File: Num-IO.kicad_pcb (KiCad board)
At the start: 2 copper layers, 170.2 x 77.5 mm, 105 parts, among them J1 DB37_Female, J2 DB37_Male, J3 Conn_02x25_Odd_Even, J4 0826-1X1T-GH-F, U1 MAX14917AFM+, U10 LTC6820HMS, U11 LTC6820HMS, U12 LTC6820HMS, U2 MAX14917AFM+, U3 MAX14851AEE+, U4 MAX14917AFM+, U5 MAX31910AUI+, U6 MAX31910AUI+, U7 MAX31910AUI+, U8 MAX31910AUI+, U9 LTC6820HMS

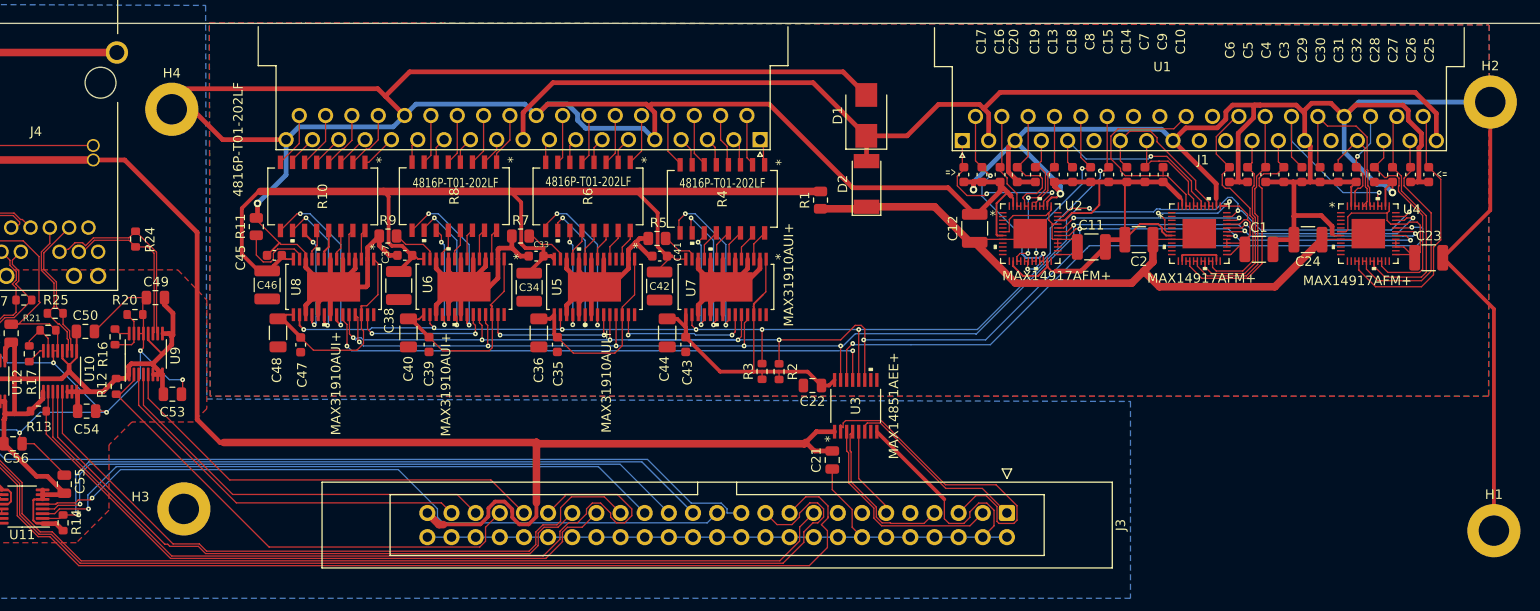
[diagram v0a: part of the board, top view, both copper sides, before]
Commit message: add missing LDO for 3.3V
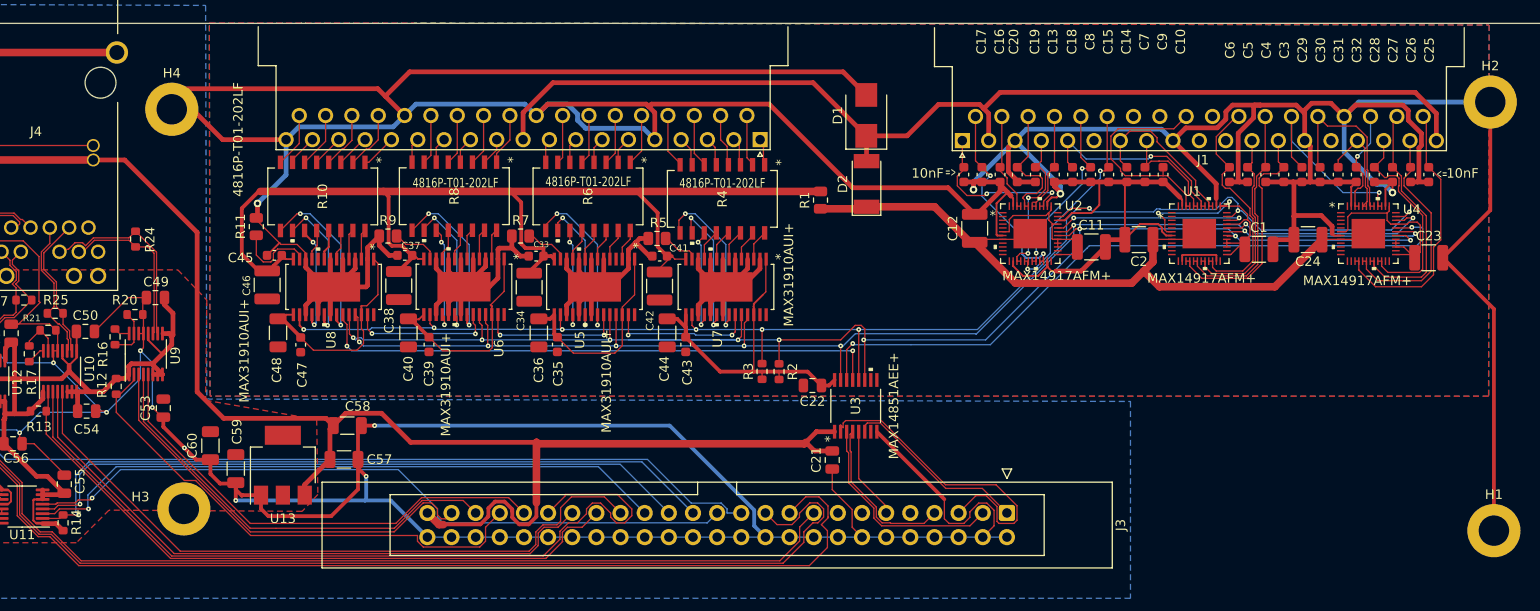
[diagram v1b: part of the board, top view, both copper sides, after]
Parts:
- added C57: 10uF, Capacitor_SMD:C_1206_3216Metric, F.Cu at (103.1, 70.1)
- added C58: 10uF, Capacitor_SMD:C_1206_3216Metric, F.Cu at (103.4, 66.5)
- added C59: 10uF, Capacitor_SMD:C_1206_3216Metric, F.Cu at (91.7, 71.1)
- added C60: 10uF, Capacitor_SMD:C_1206_3216Metric, F.Cu at (89.0, 68.7)
- added U13: AP1117-33, Package_TO_SOT_SMD:SOT-223-3_TabPin2, F.Cu at (96.6, 70.7)
- moved C53 1.75 mm to (84.1, 64.7), turned to -90 degrees
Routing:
- net GNDD: track 229.9 -> 343.2 mm, vias 7 -> 11
- net +5VD: track 139.8 -> 147.8 mm
- net /FPGA Connector/SPI4.SDO: track 40.8 -> 45.2 mm
- net /FPGA Connector/SPI4.*CS: track 47.0 -> 50.7 mm
- net /FPGA Connector/SPI4.CLK: track 42.9 -> 46.2 mm
- net +3.3V: track 107.6 -> 105.5 mm
- net /FPGA Connector/SPI4.SDI: track 52.4 -> 53.9 mm

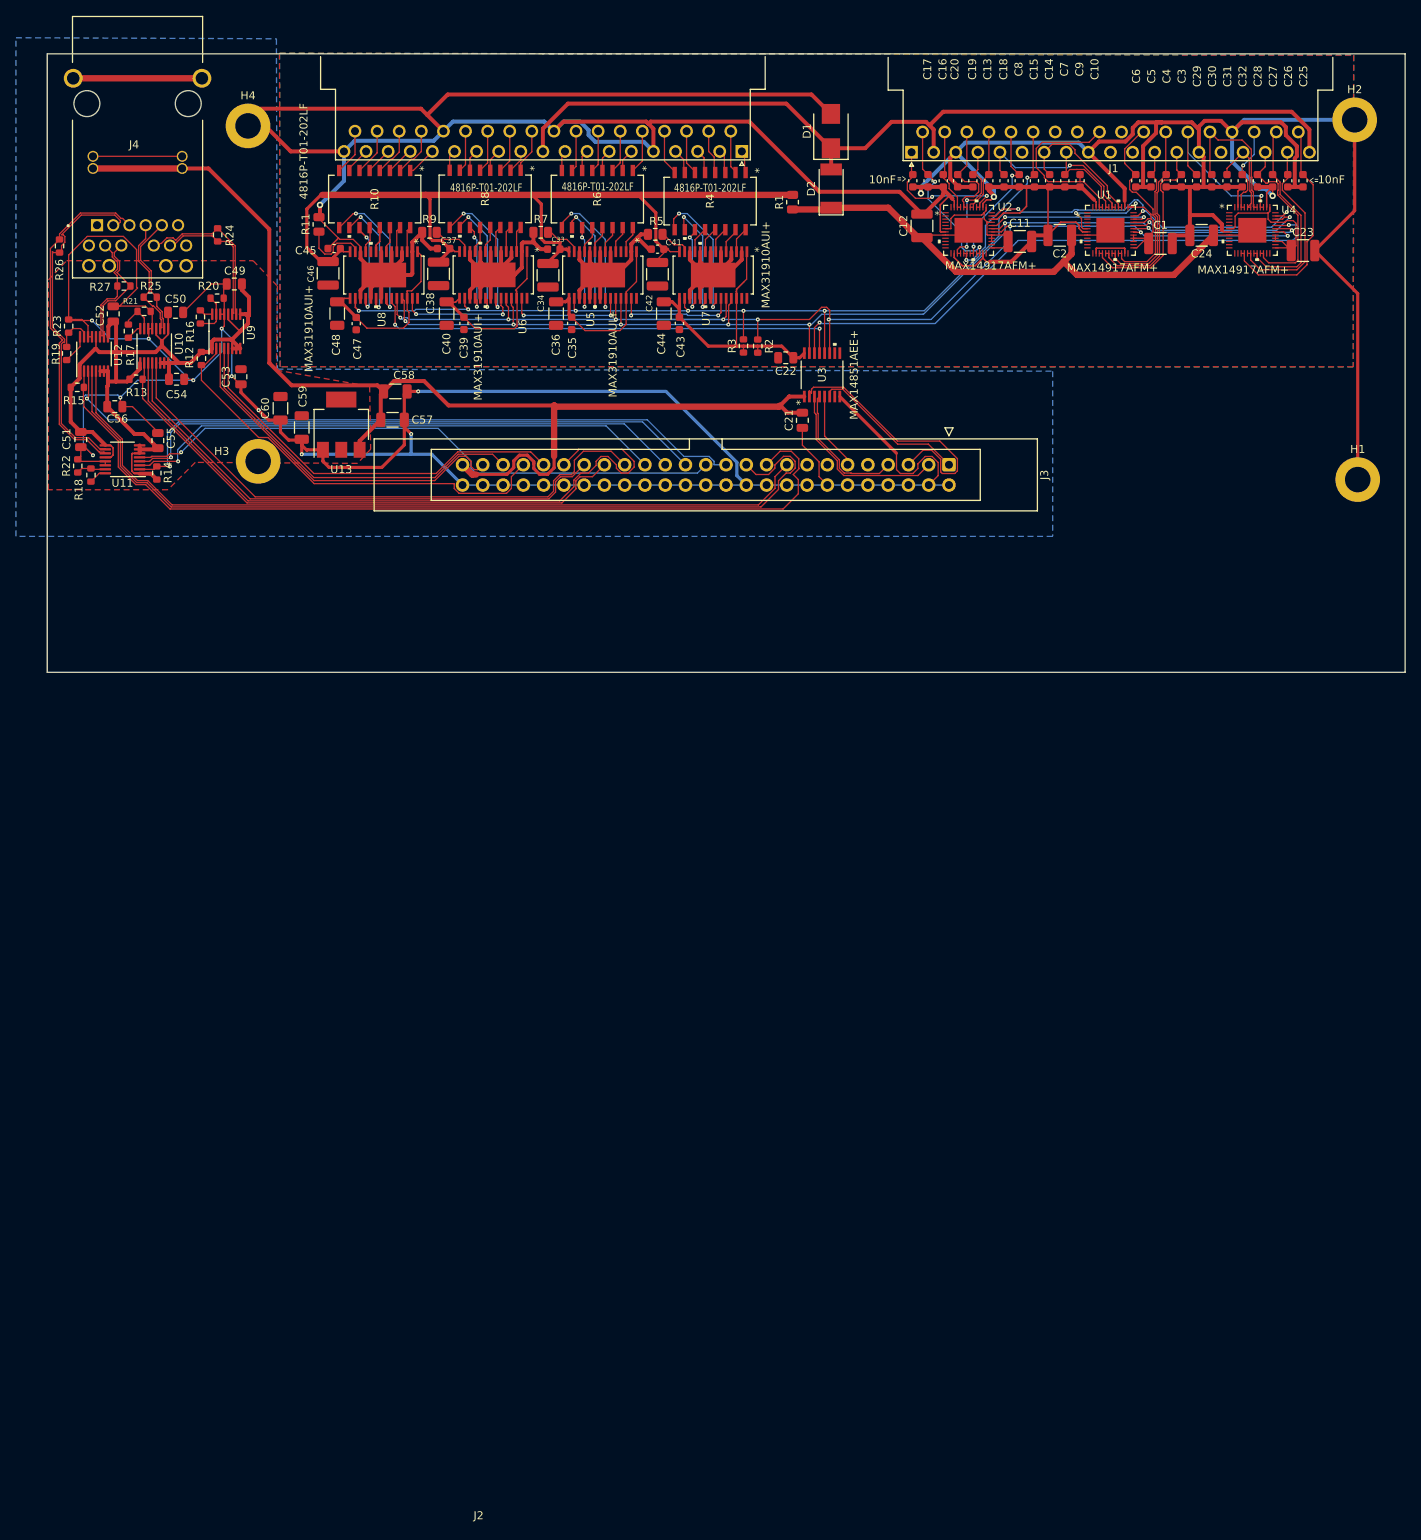
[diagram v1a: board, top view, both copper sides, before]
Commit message: fix a few warnings
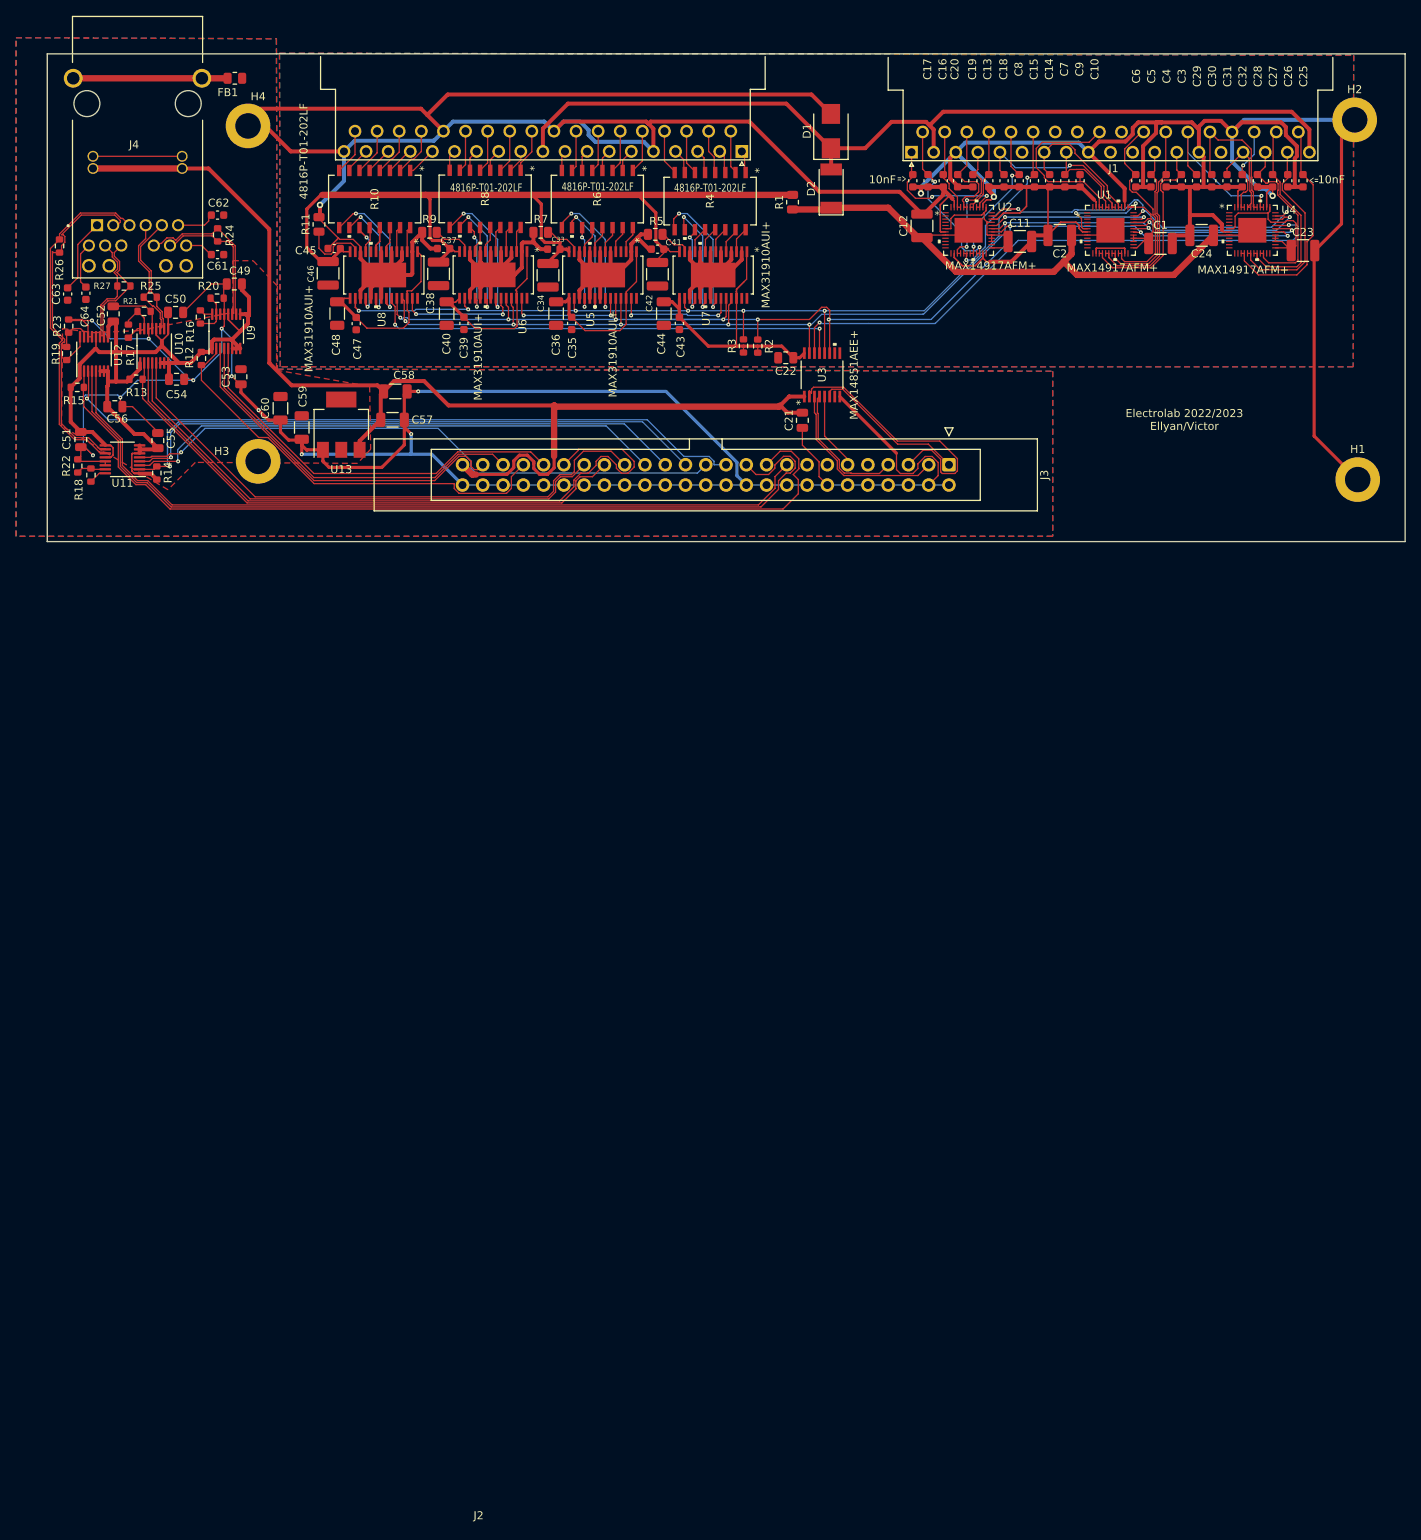
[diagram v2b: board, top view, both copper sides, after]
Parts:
- added C61: <27pF, Capacitor_SMD:C_0603_1608Metric, F.Cu at (81.1, 49.4)
- added C62: <27pF, Capacitor_SMD:C_0603_1608Metric, F.Cu at (81.1, 44.5)
- added C63: <27pF, Capacitor_SMD:C_0603_1608Metric, F.Cu at (62.4, 54.3)
- added C64: <27pF, Capacitor_SMD:C_0603_1608Metric, F.Cu at (64.6, 54.2)
- added FB1: FerriteBead, Resistor_SMD:R_0805_2012Metric, F.Cu at (83.3, 27.3)
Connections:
- net +3.3V renamed +3V3
- net Earth renamed Net-(FB1-Pad2)
- J4 pad 1: unconnected-(J4-Pad1) -> Net-(J4-Pad1)
- J4 pad 12: unconnected-(J4-Pad12) -> Net-(J4-Pad12)
- J4 pad 6: unconnected-(J4-Pad6) -> Net-(J4-Pad6)
- J4 pad 7: unconnected-(J4-Pad7) -> Net-(J4-Pad7)
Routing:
- net GNDD: track 343.2 -> 316.8 mm
- net Net-(J4-Pad1): track 0.00 -> 9.37 mm
- net Net-(J4-Pad7): track 0.00 -> 5.92 mm
- net Net-(J4-Pad6): track 0.00 -> 4.41 mm
- net Net-(J4-Pad12): track 0.00 -> 3.37 mm
- net Net-(FB1-Pad2): track 16.1 -> 19.3 mm
- added copper zone on F.Cu, net GNDD
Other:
- board size 170.2 x 77.5 mm -> 170.2 x 61.1 mm
- board text added: "Electrolab 2022/2023 Ellyan/Victor"

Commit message: fix most errors/warnings
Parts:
- added R28: 100k, Resistor_SMD:R_0603_1608Metric, F.Cu at (182.4, 44.7)
- added R29: 100k, Resistor_SMD:R_0603_1608Metric, F.Cu at (158.7, 69.7)
- added R30: 3.3k, Resistor_SMD:R_0603_1608Metric, F.Cu at (158.9, 58.8)
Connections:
- U2 pad 34: GNDPWR -> /output channel 17-24/SDO
- U3 pad 10: unconnected-(U3-Pad10) -> Net-(U3-Pad10)
- U3 pad 7: unconnected-(U3-Pad7) -> Net-(U3-Pad7)
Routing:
- net GNDPWR: track 653.7 -> 646.2 mm
- net /output channel 17-24/SDO: track 0.00 -> 3.98 mm
- net Net-(U3-Pad10): track 0.00 -> 2.28 mm
- net Net-(U3-Pad7): track 0.00 -> 2.28 mm

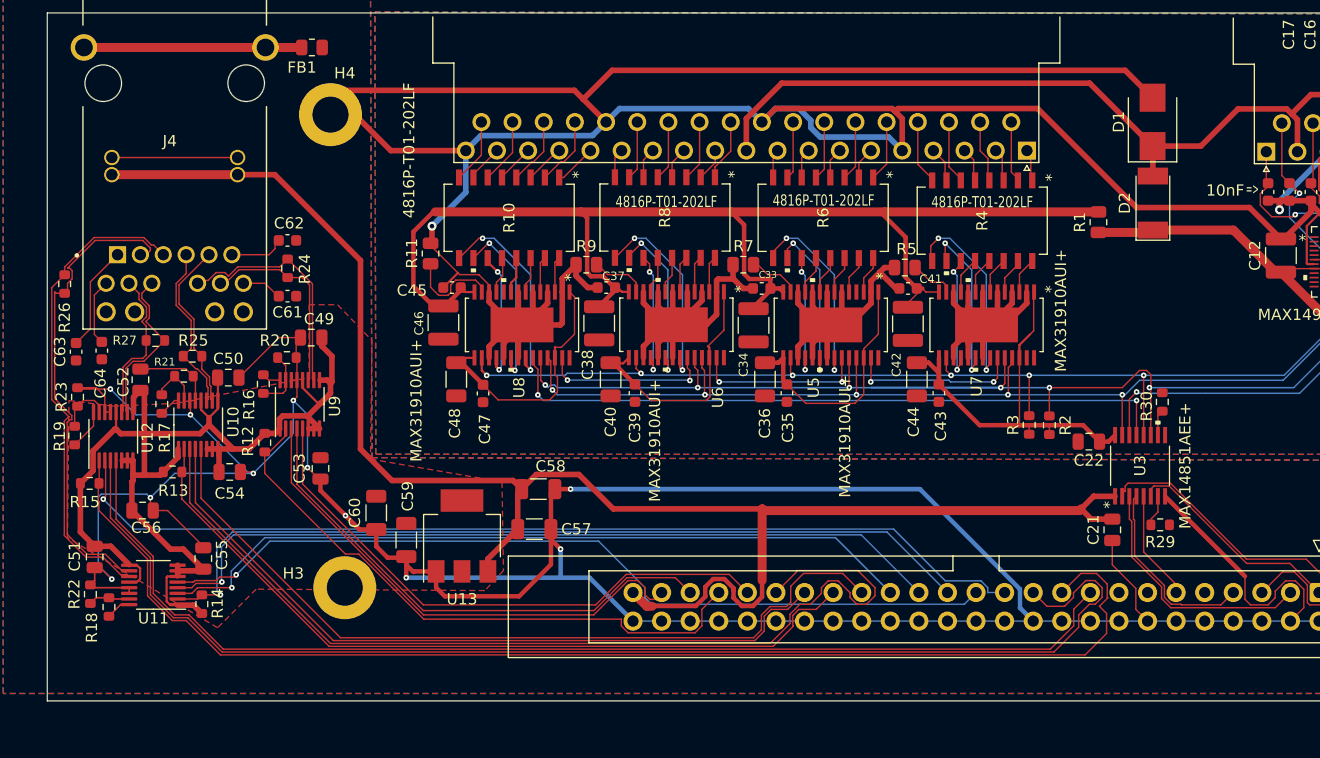
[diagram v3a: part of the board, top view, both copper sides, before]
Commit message: add KK connectors for power (check voltage or bypass)
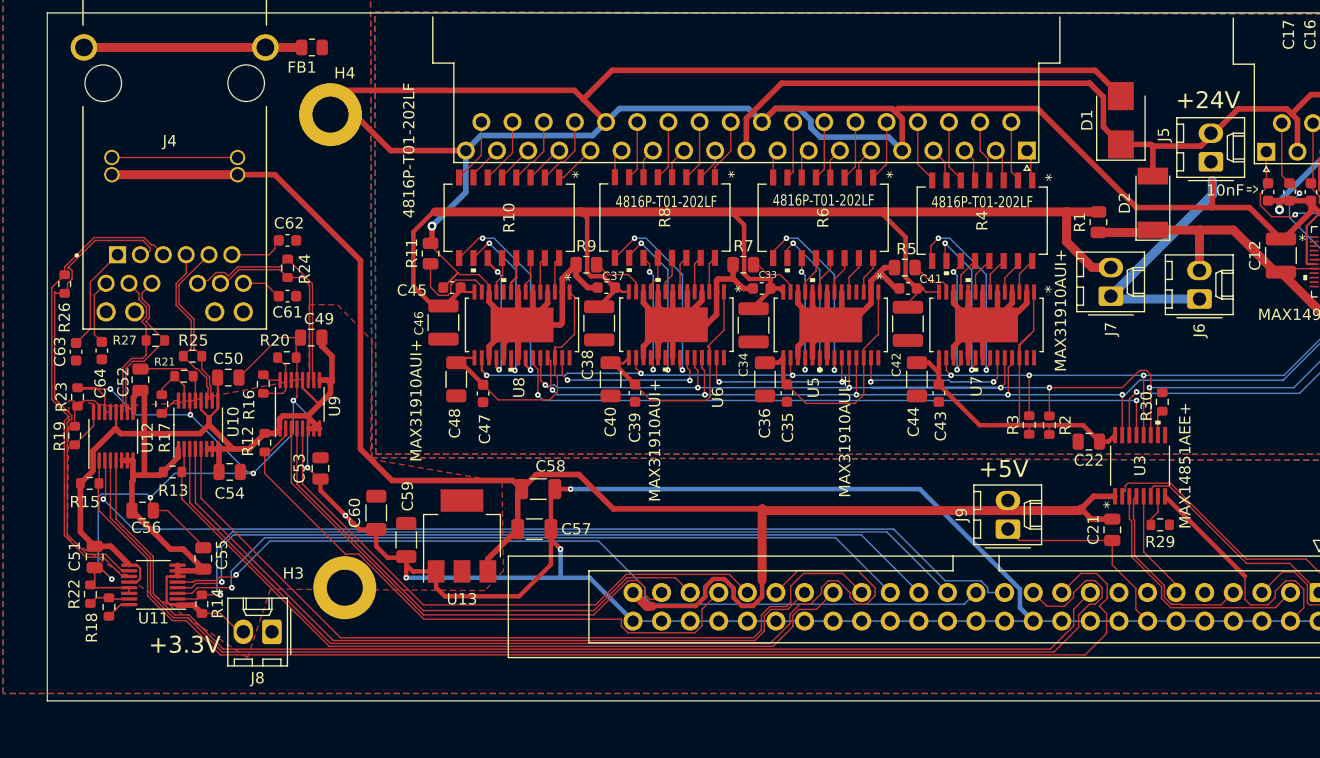
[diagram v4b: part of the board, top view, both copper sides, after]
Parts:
- added J5: Conn_01x02_Male, Connector_Molex:Molex_KK-254_AE-6410-02A_1x02_P2.54mm_Vertical, F.Cu at (163.2, 37.5)
- added J6: Conn_01x02_Male, Connector_Molex:Molex_KK-254_AE-6410-02A_1x02_P2.54mm_Vertical, F.Cu at (162.2, 49.7)
- added J7: Conn_01x02_Male, Connector_Molex:Molex_KK-254_AE-6410-02A_1x02_P2.54mm_Vertical, F.Cu at (154.3, 49.4)
- added J8: Conn_01x02_Male, Connector_Molex:Molex_KK-254_AE-6410-02A_1x02_P2.54mm_Vertical, F.Cu at (79.8, 79.2)
- added J9: Conn_01x02_Male, Connector_Molex:Molex_KK-254_AE-6410-02A_1x02_P2.54mm_Vertical, F.Cu at (145.2, 70.1)
- moved D1 2.82 mm to (155.2, 33.8)
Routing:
- net GNDPWR: track 646.2 -> 667.8 mm
- net GNDD: track 316.8 -> 326.5 mm
- net INPWR: track 111.0 -> 118.5 mm
- net +3V3: track 105.5 -> 109.8 mm
- net OUTPWR: track 78.5 -> 82.1 mm
- net +24V: track 114.8 -> 116.4 mm
- net +5VD: track 147.8 -> 148.7 mm
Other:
- board text added: "+24V"
- board text added: "+3.3V"
- board text added: "+5V"
